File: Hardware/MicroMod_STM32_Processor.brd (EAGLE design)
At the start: 22 x 22 mm, 43 parts, among them J1 MICROMOD-2222, U1 STM32F405RGT6, U3 W25QXX128MBIT-6X5, Y1 12MHz, Y2 32.768kHz

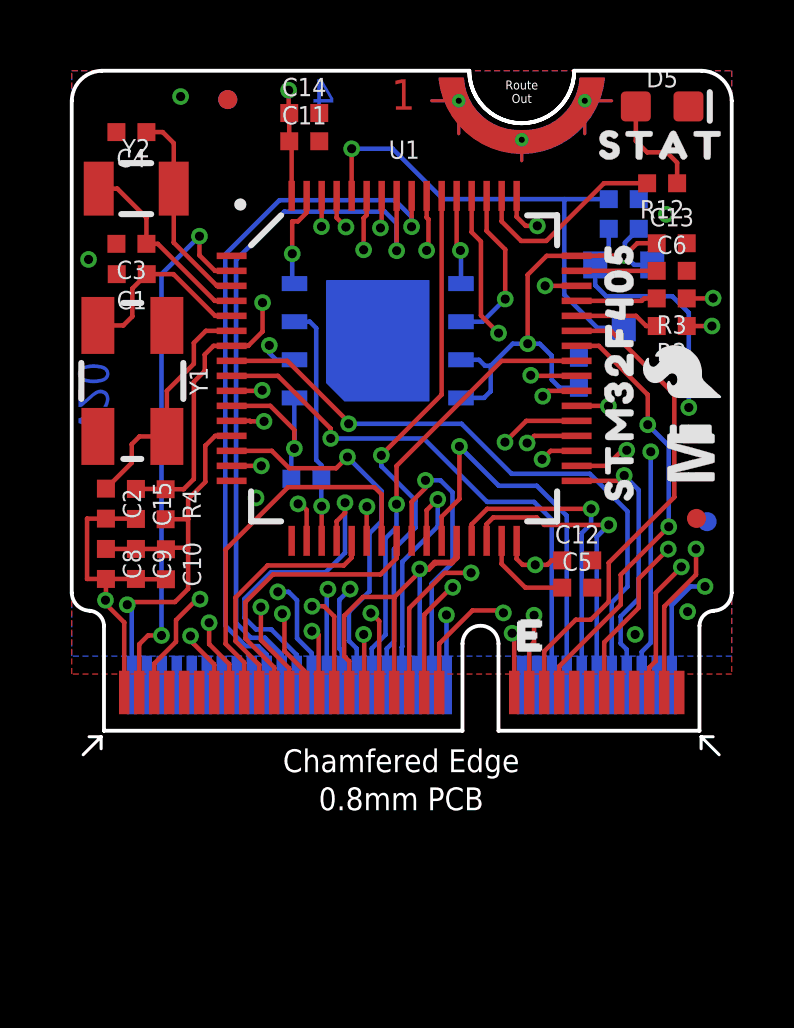
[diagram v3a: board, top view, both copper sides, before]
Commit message: Updated from current libraries. Removed R4.
Reset PUR unneeded per STM32 App Note AN4488.
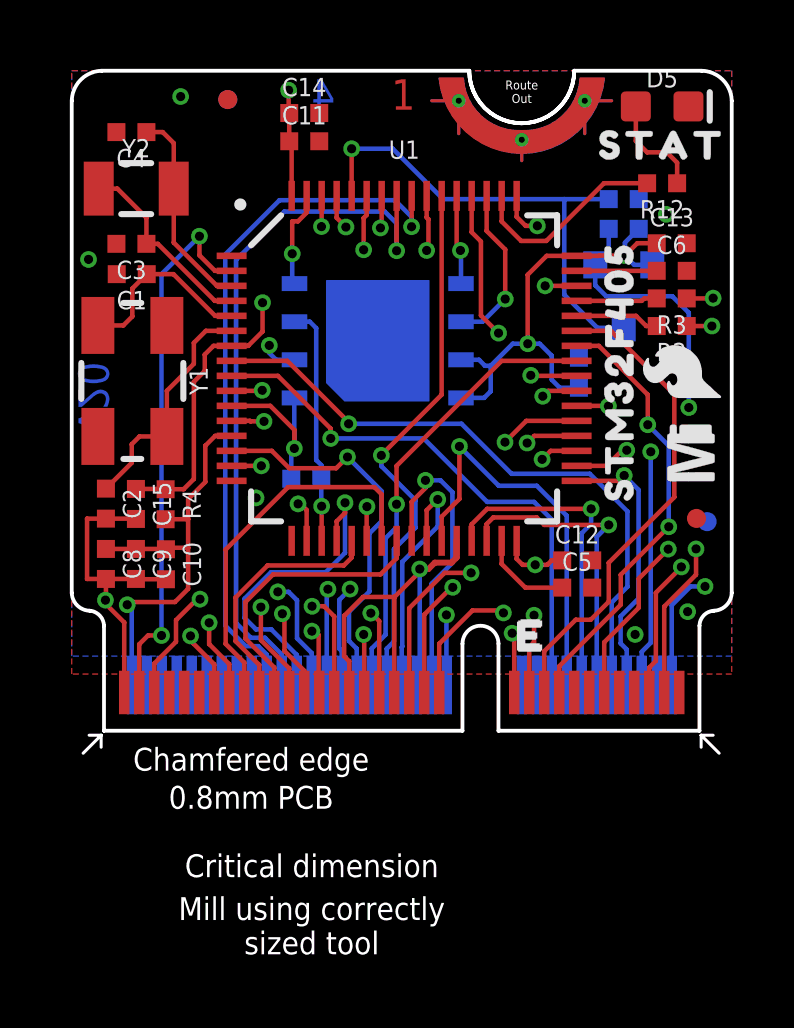
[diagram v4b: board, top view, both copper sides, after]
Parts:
- Q1: value (none) -> 20V/4.2A/52mΩ/1.4W
- R2, R3: value 22 -> 22Ω
- R4: value 5.1k -> DNP; device SparkFun-Resistors:0402-TIGHT -> SparkFun-Resistors:0402-TIGHT_NO_CREAM
